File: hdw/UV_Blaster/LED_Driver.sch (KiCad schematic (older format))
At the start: 25 parts

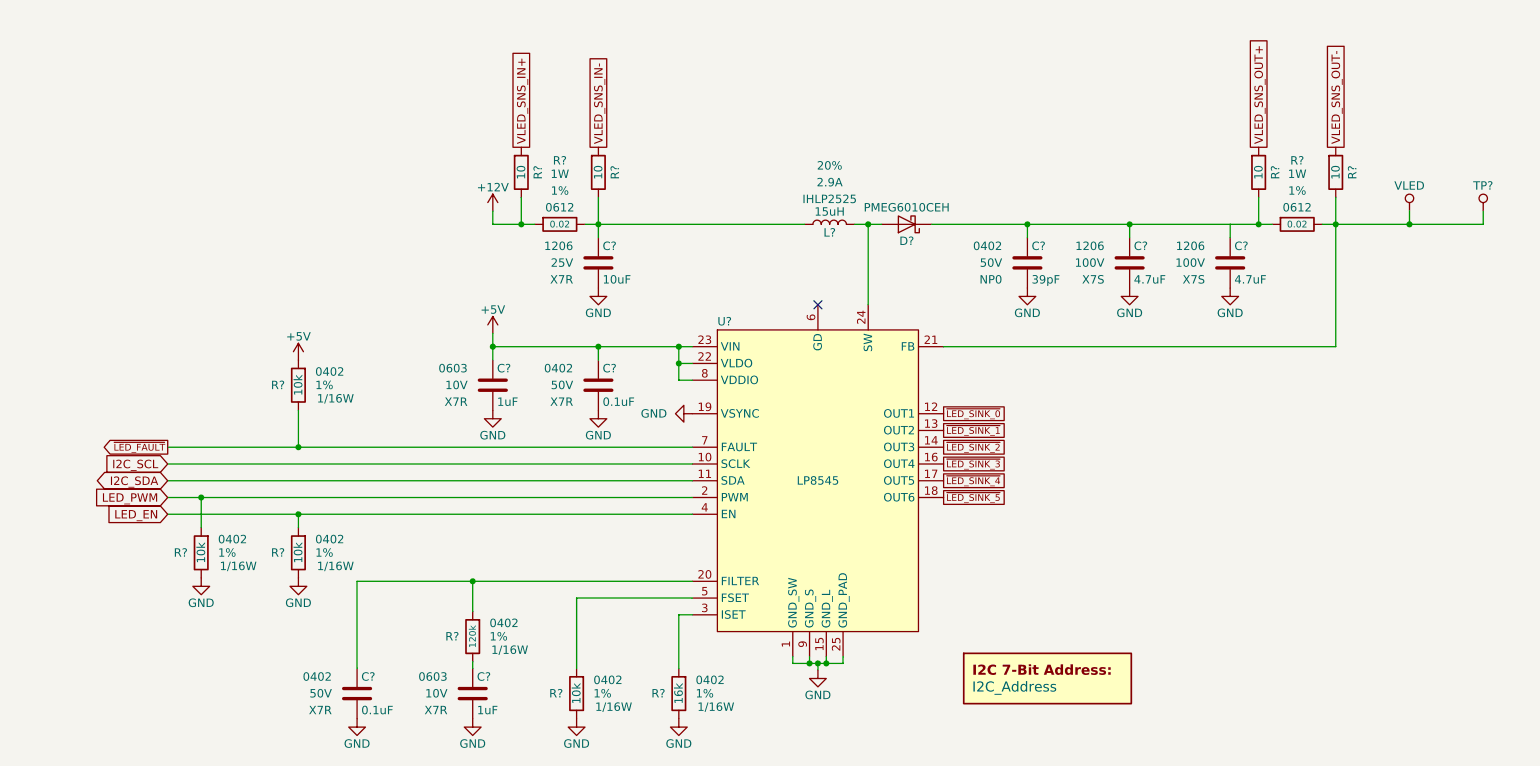
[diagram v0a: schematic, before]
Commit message: More sch work, netlist, part numbers, footprints
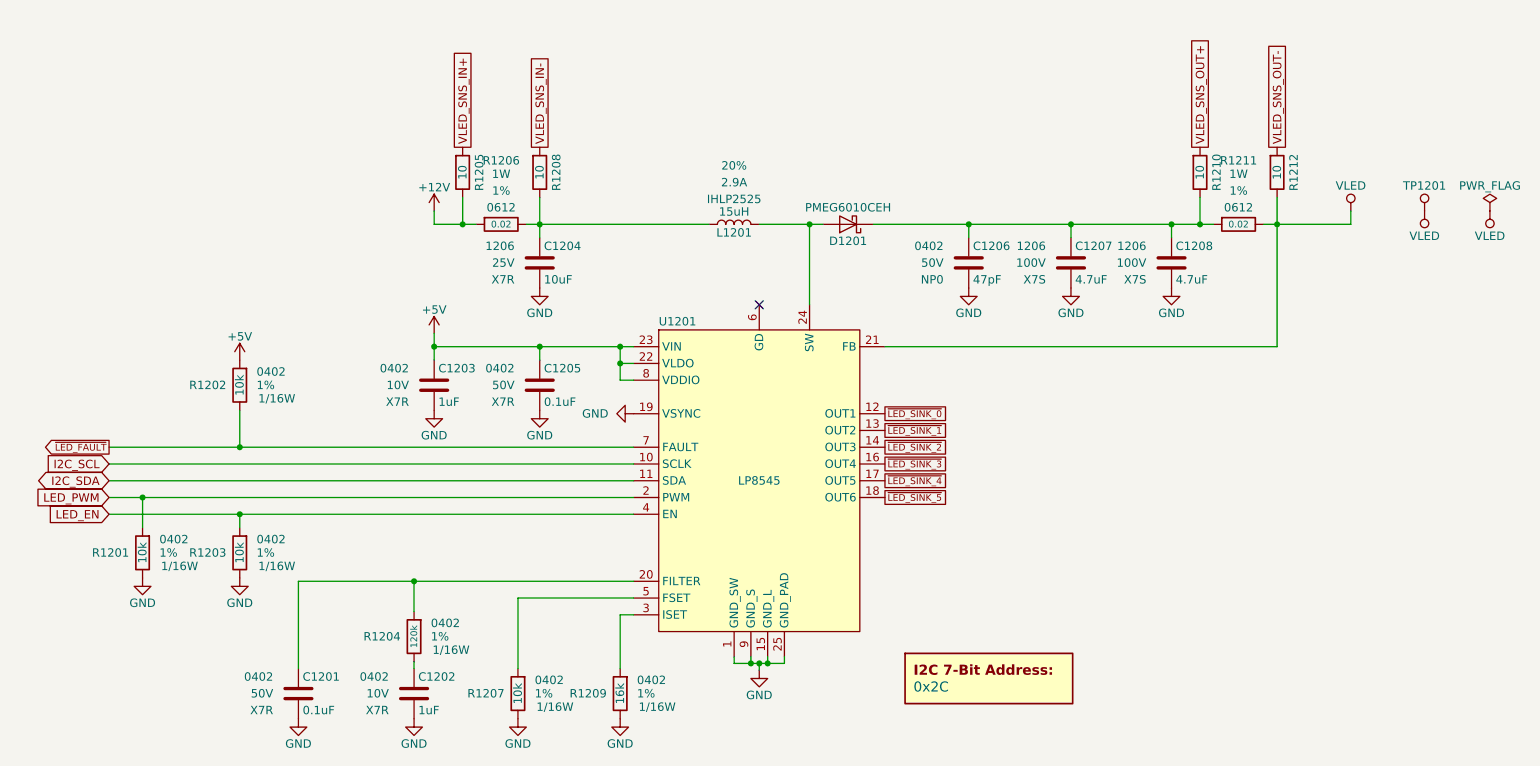
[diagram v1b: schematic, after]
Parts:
- removed C?: 39pF, symbol Custom_Library:C_Custom
- removed U?: LP8545, symbol Custom_Library:LP8545
- added C1206: 47pF, Capacitors_SMD:C_0402, symbol Custom_Library:C_Custom
- added U1201: LP8545, Housings_DFN_QFN:QFN-24-1EP_4x4mm_Pitch0.5mm, symbol Custom_Library:LP8545
- C1202, C1203: renamed from C?; footprint (none) -> Capacitors_SMD:C_0402; Digi-Key PN PN -> 490-13409-1-ND; display_footprint 0603 -> 0402
- C1204, C1207, C1208: renamed from C?; footprint (none) -> Capacitors_SMD:C_1206
- D1201: renamed from D?; Digi-Key PN (none) -> 1727-3848-1-ND
- DOC1201: renamed from DOC?; value I2C_Address -> 0x2C
- L1201: renamed from L?; Digi-Key PN (none) -> 541-2173-1-ND
- R1201, R1202, R1203, R1207: renamed from R?; Digi-Key PN (none) -> 541-3959-1-ND
- R1204: renamed from R?; Digi-Key PN (none) -> A129652CT-ND
- R1205, R1208, R1210, R1212: renamed from R?; Configuration (none) -> Telemetry; Digi-Key PN (none) -> 311-10.0LRCT-ND
- R1209: renamed from R?; Digi-Key PN (none) -> RMCF0402FT16K0CT-ND
- gave numbers to parts that had none: 5
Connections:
- net +5V: now also U1201.22 (VLDO), U1201.23 (VIN), U1201.8 (VDDIO)
- net GND: now also C1206.2, U1201.1 (GND_SW), U1201.15 (GND_L), U1201.19 (VSYNC), U1201.25 (GND_PAD), U1201.9 (GND_S)
- net I2C_SCL: now also U1201.10 (SCLK)
- net I2C_SDA: now also U1201.11 (SDA)
- net LED_EN: now also U1201.4 (EN)
- net LED_PWM: now also U1201.2 (PWM)
- net VLED: now also U1201.21 (FB)
- net ~LED_FAULT: now also U1201.7 (FAULT)
- net ~LED_SINK_0: now also U1201.12 (OUT1)
- net ~LED_SINK_1: now also U1201.13 (OUT2)
- net ~LED_SINK_2: now also U1201.14 (OUT3)
- net ~LED_SINK_3: now also U1201.16 (OUT4)
- net ~LED_SINK_4: now also U1201.17 (OUT5)
- net ~LED_SINK_5: now also U1201.18 (OUT6)
- net at C1201.1, R1204.1: now also U1201.20 (FILTER)
- net at D1201.2 (A), L1201.2: now also U1201.24 (SW)
- net at R1209.1: now also U1201.3 (ISET)
- net at R1207.1: now also U1201.5 (FSET)
- net at C1207.1, C1208.1, D1201.1 (K)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: now also C1206.1
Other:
- moved on the sheet: C1201, C1202, C1203, C1204, C1205, C1207, C1208, D1201, L1201, R1201, R1202, R1203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
